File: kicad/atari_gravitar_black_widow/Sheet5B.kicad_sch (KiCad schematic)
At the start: 23 parts

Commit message: TEST POINTS PLACED
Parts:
- added TP~{VRAM}1: TP, quantum_arcade_pcb:TP, symbol atari_grav_bw:TP
- TPSAEN1: footprint (none) -> quantum_arcade_pcb:TP
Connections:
- net ~{VRAM}: now also TP~{VRAM}1.1, TP~{VRAM}1.2
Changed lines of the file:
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@@
   (junction (at 479.425 65.405) (diameter 0) (color 0 0 0 0)
+  )
+  (junction (at 203.835 208.28) (diameter 0) (color 0 0 0 0)
   )
   (junction (at 501.65 78.105) (diameter 0) (color 0 0 0 0)
@@
     (stroke (width 0) (type default) (color 0 0 0 0))
   )
+  (wire (pts (xy 218.44 201.93) (xy 218.44 208.28))
+    (stroke (width 0) (type default) (color 0 0 0 0))
+  )
+  (wire (pts (xy 200.025 208.28) (xy 203.835 208.28))
+    (stroke (width 0) (type default) (color 0 0 0 0))
+  )
   (wire (pts (xy 474.98 45.72) (xy 474.98 48.26))
     (stroke (width 0) (type default) (color 0 0 0 0))
@@
   )
   (wire (pts (xy 63.5 118.11) (xy 63.5 72.39))
+    (stroke (width 0) (type default) (color 0 0 0 0))
+  )
+  (wire (pts (xy 203.835 208.28) (xy 218.44 208.28))
     (stroke (width 0) (type default) (color 0 0 0 0))
   )
@@
     (pin "1")
   )
+  (symbol (lib_id "atari_grav_bw:TP") (at 201.93 203.2 0) (unit 1)
+    (in_bom yes) (on_board yes)
+    (property "Reference" "TP~{VRAM}1" (id 0) (at 191.6684 201.8792 0)
+      (effects (font (size 1.524 1.524)) (justify left))
+    )
+    (property "Value" "TP" (id 1) (at 200.025 201.93 0)
+      (effects (font (size 1.524 1.524)) hide)
+    )
+    (property "Footprint" "quantum_arcade_pcb:TP" (id 2) (at 200.025 204.47 0)
+      (effects (font (size 1.524 1.524)) hide)
+    )
+    (property "Datasheet" "" (id 3) (at 200.025 204.47 0)
+      (effects (font (size 1.524 1.524)) hide)
+    )
+    (pin "1")
+    (pin "2")
+  )
   (symbol (lib_id "power:GND") (at 97.155 116.205 0) (unit 1)
     (in_bom yes) (on_board yes)
@@
       (effects (font (size 1.524 1.524)) hide)
     )
-    (property "Footprint" "" (id 2) (at 145.669 223.52 0)
+    (property "Footprint" "quantum_arcade_pcb:TP" (id 2) (at 145.669 223.52 0)
       (effects (font (size 1.524 1.524)) hide)
     )

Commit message: TP vrom creation
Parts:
- added TP? (x4): TP, symbol atari_grav_bw:TP
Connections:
- net ~{VROM3}: now also TP?.2
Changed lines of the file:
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@@
   (junction (at 488.315 45.72) (diameter 0) (color 0 0 0 0)
+  )
+  (junction (at 192.8876 91.44) (diameter 0) (color 0 0 0 0)
   )
   (junction (at 497.205 45.72) (diameter 0) (color 0 0 0 0)
@@
   (no_connect (at 109.22 90.17))
   (no_connect (at 109.22 95.25))
+  (wire (pts (xy 192.8876 91.44) (xy 196.215 91.44))
+    (stroke (width 0) (type default) (color 0 0 0 0))
+  )
   (wire (pts (xy 93.853 242.57) (xy 96.901 242.57))
     (stroke (width 0) (type default) (color 0 0 0 0))
@@
     (stroke (width 0) (type default) (color 0 0 0 0))
   )
+  (wire (pts (xy 192.8876 91.44) (xy 192.8876 100.9142))
+    (stroke (width 0) (type default) (color 0 0 0 0))
+  )
   (wire (pts (xy 88.265 191.135) (xy 94.615 191.135))
     (stroke (width 0) (type default) (color 0 0 0 0))
@@
     (stroke (width 0) (type default) (color 0 0 0 0))
   )
+  (wire (pts (xy 178.3842 100.9142) (xy 178.3842 100.9396))
+    (stroke (width 0) (type default) (color 0 0 0 0))
+  )
   (polyline (pts (xy 29.845 22.225) (xy 29.845 130.81))
     (stroke (width 0) (type default) (color 0 0 0 0))
@@
     (stroke (width 0) (type default) (color 0 0 0 0))
   )
+  (wire (pts (xy 192.8876 100.9142) (xy 178.3842 100.9142))
+    (stroke (width 0) (type default) (color 0 0 0 0))
+  )
   (wire (pts (xy 473.075 78.105) (xy 501.65 78.105))
     (stroke (width 0) (type default) (color 0 0 0 0))
@@
     (stroke (width 0) (type default) (color 0 0 0 0))
   )
-  (wire (pts (xy 188.595 91.44) (xy 196.215 91.44))
-    (stroke (width 0) (type default) (color 0 0 0 0))
-  )
   (wire (pts (xy 63.5 118.11) (xy 63.5 72.39))
     (stroke (width 0) (type default) (color 0 0 0 0))
@@
   )
   (polyline (pts (xy 564.515 28.575) (xy 564.515 105.41))
+    (stroke (width 0) (type default) (color 0 0 0 0))
+  )
+  (wire (pts (xy 188.595 91.44) (xy 192.8876 91.44))
     (stroke (width 0) (type default) (color 0 0 0 0))
   )
@@
     (pin "1")
   )
+  (symbol (lib_id "atari_grav_bw:TP") (at 237.7948 98.2218 0) (unit 1)
+    (in_bom yes) (on_board yes) (fields_autoplaced)
+    (property "Reference" "TP?" (id 0) (at 240.4618 96.3168 0)
+      (effects (font (size 1.524 1.524)) (justify left))
+    )
+    (property "Value" "TP" (id 1) (at 235.8898 96.9518 0)
+      (effects (font (size 1.524 1.524)) hide)
+    )
+    (property "Footprint" "" (id 2) (at 235.8898 99.4918 0)
+      (effects (font (size 1.524 1.524)) hide)
+    )
+    (property "Datasheet" "" (id 3) (at 235.8898 99.4918 0)
+      (effects (font (size 1.524 1.524)) hide)
+    )
+    (pin "1")
+    (pin "2")
+  )
   (symbol (lib_id "atari_grav_bw:2532B") (at 196.85 70.485 0) (unit 1)
     (in_bom yes) (on_board yes)
@@
     (pin "1")
   )
+  (symbol (lib_id "atari_grav_bw:TP") (at 176.4792 95.8342 0) (unit 1)
+    (in_bom yes) (on_board yes) (fields_autoplaced)
+    (property "Reference" "TP?" (id 0) (at 179.1462 93.9292 0)
+      (effects (font (size 1.524 1.524)) (justify left))
+    )
+    (property "Value" "TP" (id 1) (at 174.5742 94.5642 0)
+      (effects (font (size 1.524 1.524)) hide)
+    )
+    (property "Footprint" "" (id 2) (at 174.5742 97.1042 0)
+      (effects (font (size 1.524 1.524)) hide)
+    )
+    (property "Datasheet" "" (id 3) (at 174.5742 97.1042 0)
+      (effects (font (size 1.524 1.524)) hide)
+    )
+    (pin "1")
+    (pin "2")
+  )
   (symbol (lib_id "atari_grav_bw:TP") (at 201.93 203.2 0) (unit 1)
     (in_bom yes) (on_board yes)
@@
     )
     (pin "1")
+  )
+  (symbol (lib_id "atari_grav_bw:TP") (at 231.648 97.6376 0) (unit 1)
+    (in_bom yes) (on_board yes) (fields_autoplaced)
+    (property "Reference" "TP?" (id 0) (at 234.315 95.7326 0)
+      (effects (font (size 1.524 1.524)) (justify left))
+    )
+    (property "Value" "TP" (id 1) (at 229.743 96.3676 0)
+      (effects (font (size 1.524 1.524)) hide)
+    )
+    (property "Footprint" "" (id 2) (at 229.743 98.9076 0)
+      (effects (font (size 1.524 1.524)) hide)
+    )
+    (property "Datasheet" "" (id 3) (at 229.743 98.9076 0)
+      (effects (font (size 1.524 1.524)) hide)
+    )
+    (pin "1")
+    (pin "2")
   )
   (symbol (lib_id "power:+5V") (at 196.215 49.53 0) (unit 1)
@@
     (pin "4")
   )
+  (symbol (lib_id "atari_grav_bw:TP") (at 224.0788 97.155 0) (unit 1)
+    (in_bom yes) (on_board yes) (fields_autoplaced)
+    (property "Reference" "TP?" (id 0) (at 226.7458 95.25 0)
+      (effects (font (size 1.524 1.524)) (justify left))
+    )
+    (property "Value" "TP" (id 1) (at 222.1738 95.885 0)
+      (effects (font (size 1.524 1.524)) hide)
+    )
+    (property "Footprint" "" (id 2) (at 222.1738 98.425 0)
+      (effects (font (size 1.524 1.524)) hide)
+    )
+    (property "Datasheet" "" (id 3) (at 222.1738 98.425 0)
+      (effects (font (size 1.524 1.524)) hide)
+    )
+    (pin "1")
+    (pin "2")
+  )
   (symbol (lib_id "atari_grav_bw:LS32") (at 126.365 168.275 0) (unit 4) (convert 2)

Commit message: TP
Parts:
- removed TP? (x3): TP, symbol atari_grav_bw:TP
- added TP~{VROM0}1, TP~{VROM1}1, TP~{VROM2}1: TP, quantum_arcade_pcb:TP, symbol atari_grav_bw:TP
- TP~{VROM3}1: renamed from TP?; footprint (none) -> quantum_arcade_pcb:TP
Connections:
- net ~{VROM3}: no longer TP~{VROM3}1.2
- net at TP~{VROM3}1.1: now also TP~{VROM3}1.2
- new net: TP~{VROM1}1.1, TP~{VROM1}1.2
- new net: TP~{VROM0}1.1, TP~{VROM0}1.2
- new net: TP~{VROM2}1.1, TP~{VROM2}1.2

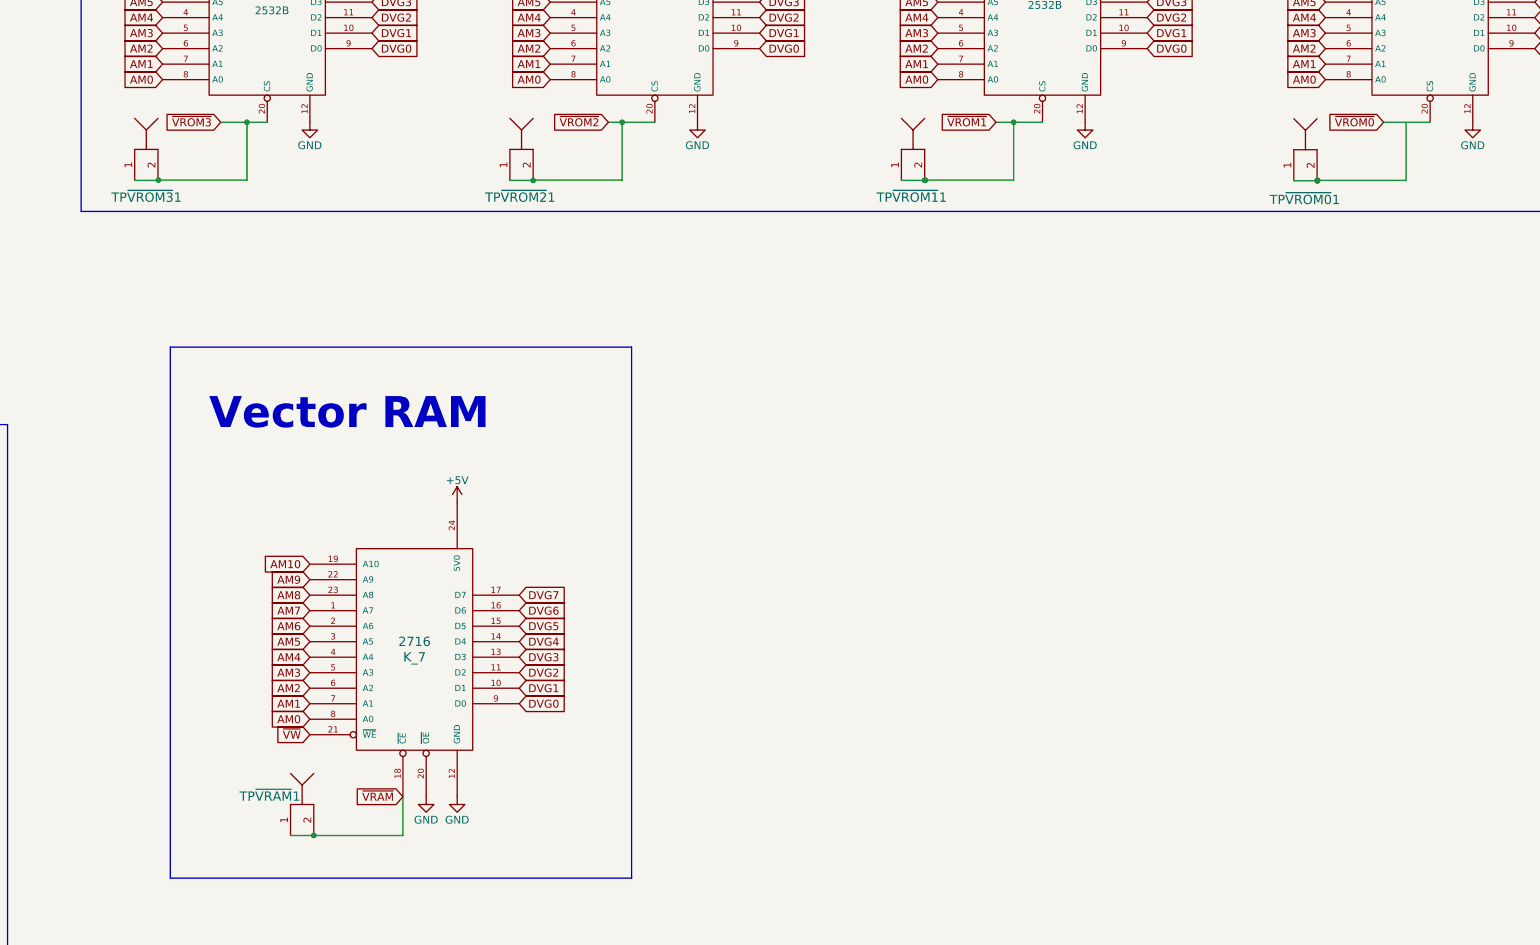
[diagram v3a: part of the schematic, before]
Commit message: Added traces and bottom image
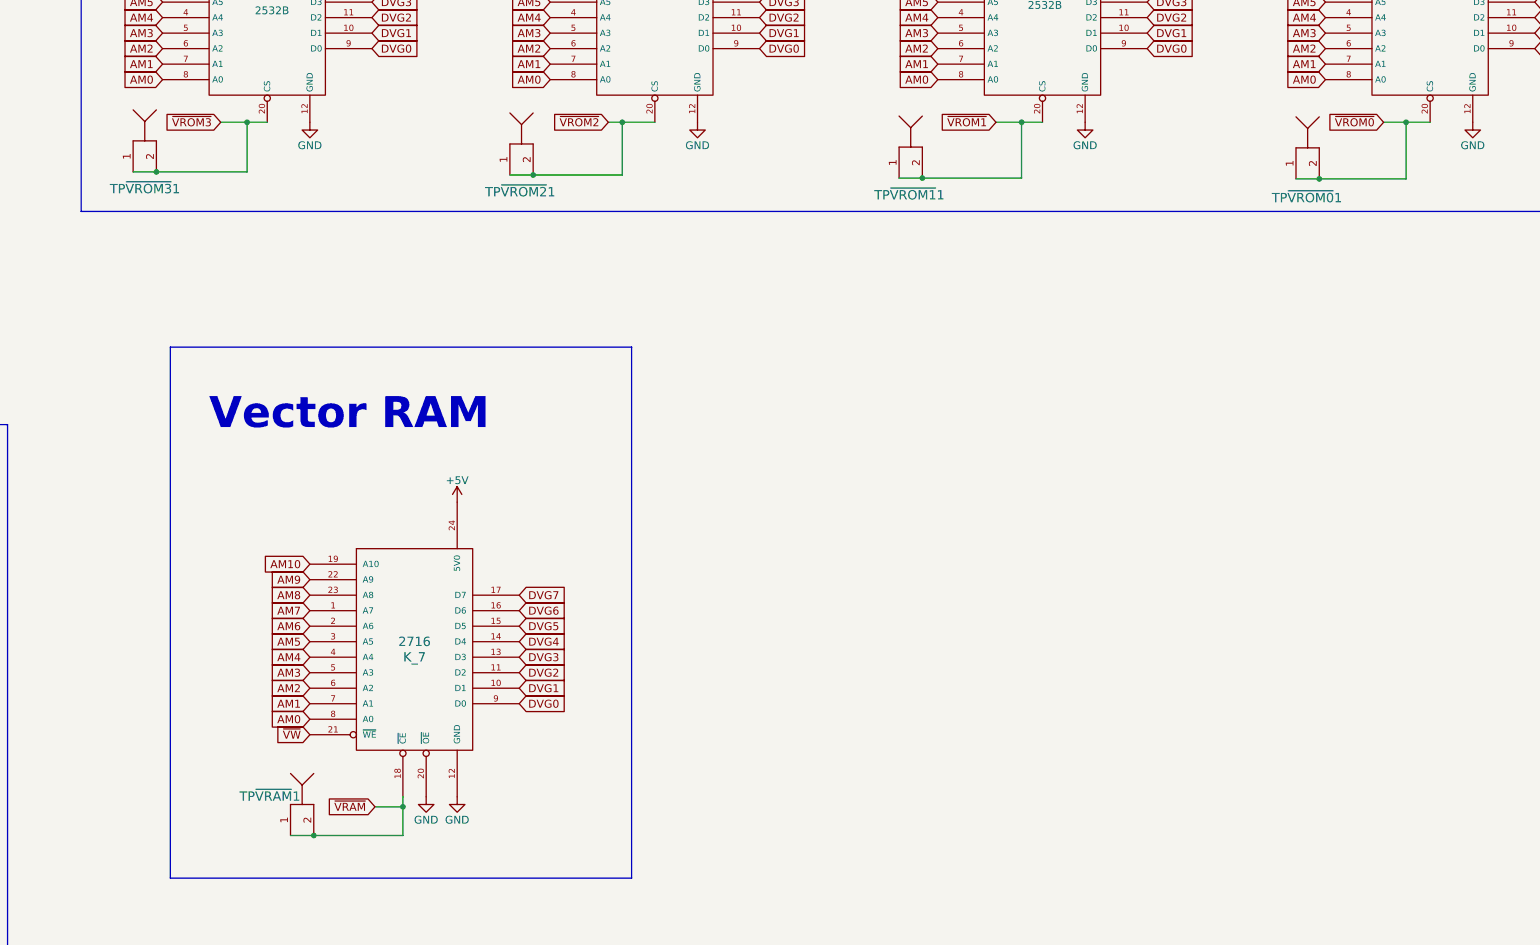
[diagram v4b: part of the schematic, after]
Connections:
- net ~{VROM0}: now also TP~{VROM0}1.1, TP~{VROM0}1.2
- net ~{VROM1}: now also TP~{VROM1}1.1, TP~{VROM1}1.2
- net ~{VROM2}: now also TP~{VROM2}1.1, TP~{VROM2}1.2
- net ~{VROM3}: now also TP~{VROM3}1.1, TP~{VROM3}1.2
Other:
- moved on the sheet: TP~{VROM1}1, TP~{VROM2}1, TP~{VROM3}1

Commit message: resistor placements R1-R153
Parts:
- R61, R62, R63, R64, R65, R66, R67, R68: footprint (none) -> Star_Wars_Vector_PCB:GenericComp
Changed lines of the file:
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@@
     (property "Reference" "R67" (id 0) (at 503.682 52.07 90))
     (property "Value" "10K" (id 1) (at 501.65 52.07 90))
-    (property "Footprint" "" (id 2) (at 499.872 52.07 90)
+    (property "Footprint" "Star_Wars_Vector_PCB:GenericComp" (id 2) (at 499.872 52.07 90)
       (effects (font (size 1.27 1.27)) hide)
     )
@@
     (property "Reference" "R61" (id 0) (at 477.012 52.07 90))
     (property "Value" "10K" (id 1) (at 474.98 52.07 90))
-    (property "Footprint" "" (id 2) (at 473.202 52.07 90)
+    (property "Footprint" "Star_Wars_Vector_PCB:GenericComp" (id 2) (at 473.202 52.07 90)
       (effects (font (size 1.27 1.27)) hide)
     )
@@
     (property "Reference" "R62" (id 0) (at 481.457 52.07 90))
     (property "Value" "10K" (id 1) (at 479.425 52.07 90))
-    (property "Footprint" "" (id 2) (at 477.647 52.07 90)
+    (property "Footprint" "Star_Wars_Vector_PCB:GenericComp" (id 2) (at 477.647 52.07 90)
       (effects (font (size 1.27 1.27)) hide)
     )
@@
     (property "Reference" "R64" (id 0) (at 490.347 52.07 90))
     (property "Value" "10K" (id 1) (at 488.315 52.07 90))
-    (property "Footprint" "" (id 2) (at 486.537 52.07 90)
+    (property "Footprint" "Star_Wars_Vector_PCB:GenericComp" (id 2) (at 486.537 52.07 90)
       (effects (font (size 1.27 1.27)) hide)
     )
@@
     (property "Reference" "R63" (id 0) (at 485.902 52.07 90))
     (property "Value" "10K" (id 1) (at 483.87 52.07 90))
-    (property "Footprint" "" (id 2) (at 482.092 52.07 90)
+    (property "Footprint" "Star_Wars_Vector_PCB:GenericComp" (id 2) (at 482.092 52.07 90)
       (effects (font (size 1.27 1.27)) hide)
     )
@@
     (property "Reference" "R65" (id 0) (at 494.792 52.07 90))
     (property "Value" "10K" (id 1) (at 492.76 52.07 90))
-    (property "Footprint" "" (id 2) (at 490.982 52.07 90)
+    (property "Footprint" "Star_Wars_Vector_PCB:GenericComp" (id 2) (at 490.982 52.07 90)
       (effects (font (size 1.27 1.27)) hide)
     )
@@
     (property "Reference" "R66" (id 0) (at 499.237 52.07 90))
     (property "Value" "10K" (id 1) (at 497.205 52.07 90))
-    (property "Footprint" "" (id 2) (at 495.427 52.07 90)
+    (property "Footprint" "Star_Wars_Vector_PCB:GenericComp" (id 2) (at 495.427 52.07 90)
       (effects (font (size 1.27 1.27)) hide)
     )
@@
     (property "Reference" "R68" (id 0) (at 508.127 52.07 90))
     (property "Value" "10K" (id 1) (at 506.095 52.07 90))
-    (property "Footprint" "" (id 2) (at 504.317 52.07 90)
-      (effects (font (size 1.27 1.27)) hide)
-    )
+    (property "Footprint" "Star_Wars_Vector_PCB:GenericComp" (id 2) (at 504.317 52.07 90)
+      (effects (font (size 1.27 1.27)) hide)
+    )

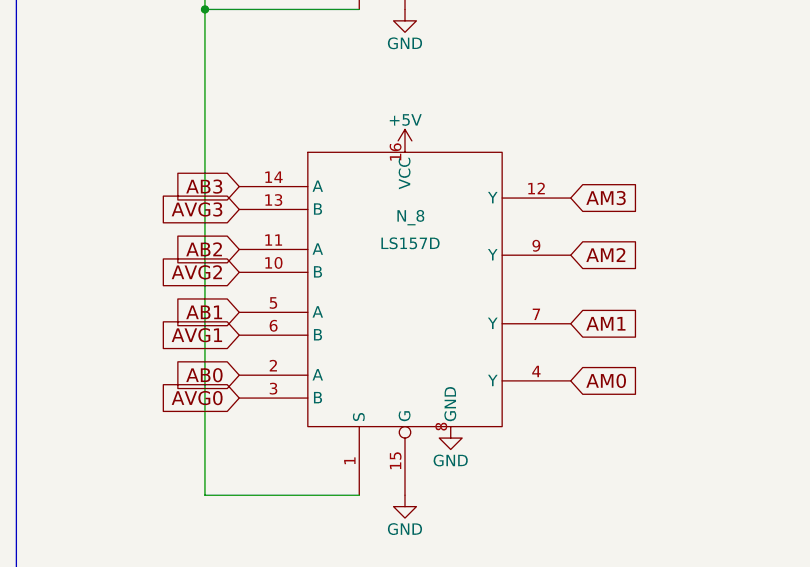
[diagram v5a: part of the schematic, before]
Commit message: Row 2 routing and schematic fixes
EAROM (M2) had duplicate pins and no footprint :(
N8 pins were in wrong order
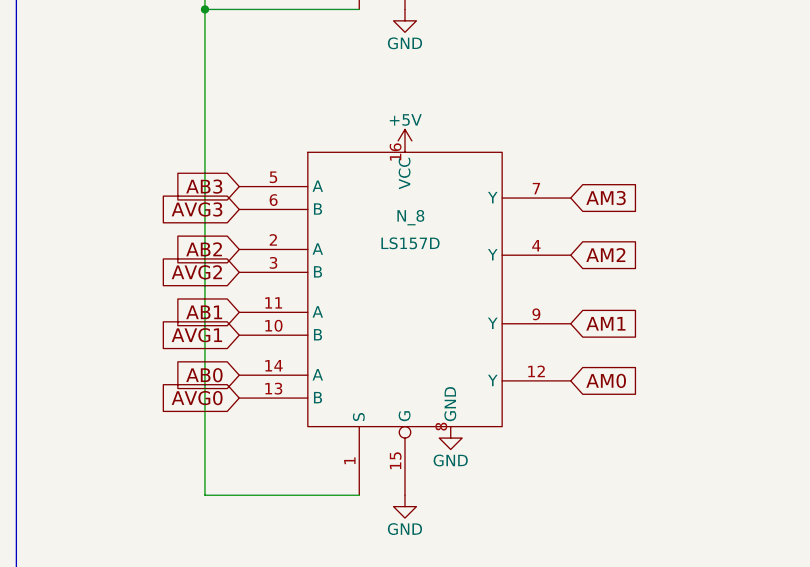
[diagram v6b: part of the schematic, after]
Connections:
- net AB0: now also N_8.14 (A); no longer N_8.2 (A)
- net AB1: now also N_8.11 (A); no longer N_8.5 (A)
- net AB2: now also N_8.2 (A); no longer N_8.11 (A)
- net AB3: now also N_8.5 (A); no longer N_8.14 (A)
- net AM0: now also N_8.12 (Y); no longer N_8.4 (Y)
- net AM1: now also N_8.9 (Y); no longer N_8.7 (Y)
- net AM2: now also N_8.4 (Y); no longer N_8.9 (Y)
- net AM3: now also N_8.7 (Y); no longer N_8.12 (Y)
- net AVG0: now also N_8.13 (B); no longer N_8.3 (B)
- net AVG1: now also N_8.10 (B); no longer N_8.6 (B)
- net AVG2: now also N_8.3 (B); no longer N_8.10 (B)
- net AVG3: now also N_8.6 (B); no longer N_8.13 (B)
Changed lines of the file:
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@@
     (pin "1")
   )
-  (symbol (lib_id "atari_grav_bw:LS157D") (at 70.485 361.95 0) (unit 1)
+  (symbol (lib_name "LS157D_1") (lib_id "atari_grav_bw:LS157D") (at 70.485 361.95 0) (unit 1)
     (in_bom yes) (on_board yes)
     (property "Reference" "N_8" (id 0) (at 68.834 354.457 0)
